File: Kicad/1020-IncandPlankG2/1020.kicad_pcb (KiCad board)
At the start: 2 copper layers, 50 x 65 mm, 33 parts, among them J1 Conn_01x22, P1 CONN_4X2, P10 CONN_2, P11 SPADE_187, P2 CONN_4X2, P3 CONN_4, P4 TST, P5 TST, P6 TST, P7 TST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

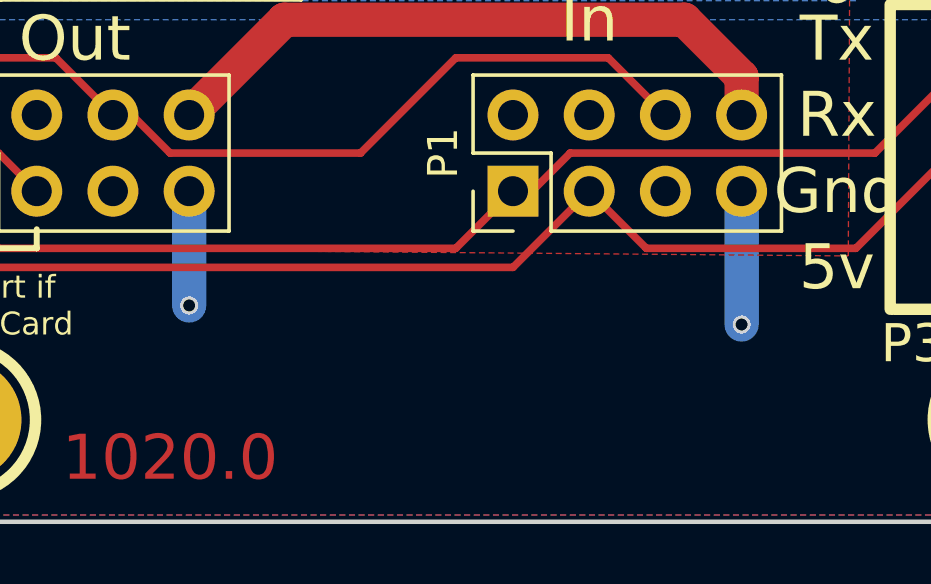
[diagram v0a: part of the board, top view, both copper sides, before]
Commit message: SolPlank:  Increase via size to meet DFM minimum.  Update build.bat to save to 1019.zip.  Add build_notes.txt to describe setting up Kicad libraries, and creating Gerbers.  Add 1019.zip for ease of ordering PCBs.
IncandPlank:  Increase via size to meet DFM minimum.  Update build.bat to save to 1020.zip.  Add build_notes.txt to describe setting up Kicad libraries, and creating Gerbers.  Add 1019.zip for ease of ordering PCBs.

VH:  Last updates grabbed from machine before sending to Joe.
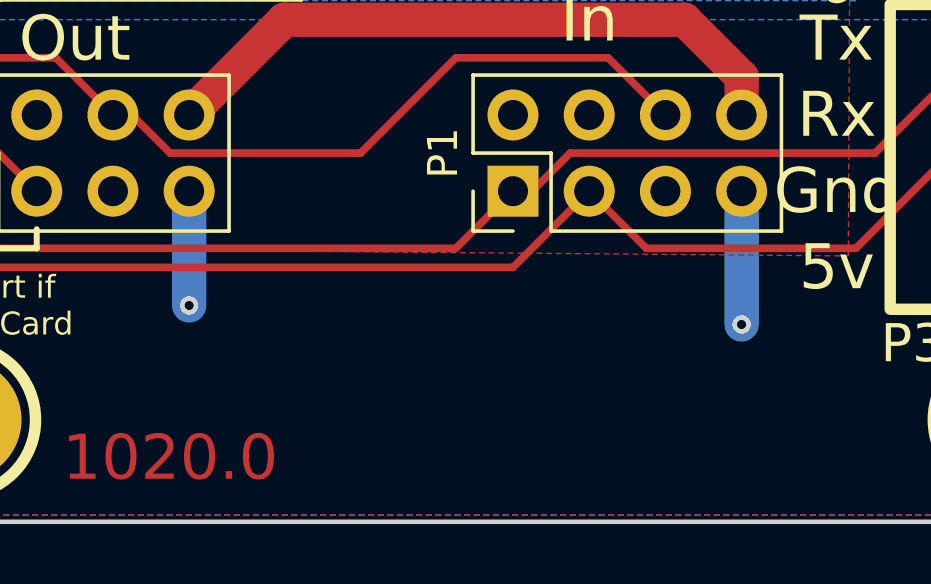
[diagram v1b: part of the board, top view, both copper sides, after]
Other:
- net class Default: via_dia 0.6 -> 0.6096; via_drill 0.4 -> 0.3048
- rule via_min_drill: 0.3 -> 0.3048
- rule via_min_size: 0.4 -> 0.6096
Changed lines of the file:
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@@
     (segment_width 0.2)
     (edge_width 0.15)
-    (via_size 0.6)
-    (via_drill 0.4)
-    (via_min_size 0.4)
-    (via_min_drill 0.3)
+    (via_size 0.6096)
+    (via_drill 0.3048)
+    (via_min_size 0.6096)
+    (via_min_drill 0.3048)
     (uvia_size 0.3)
     (uvia_drill 0.1)
@@
     (visible_elements 7FFFFFFF)
     (pcbplotparams
-      (layerselection 0x00030_80000001)
-      (usegerberextensions false)
-      (excludeedgelayer true)
+      (layerselection 0x000f0_80000001)
+      (usegerberextensions true)
+      (excludeedgelayer false)
       (linewidth 0.100000)
       (plotframeref false)
@@
       (outputformat 1)
       (mirror false)
-      (drillshape 1)
+      (drillshape 0)
       (scaleselection 1)
-      (outputdirectory ""))
+      (outputdirectory Gerber/))
   )
   (net 0 "")
@@
     (clearance 0.2)
     (trace_width 0.25)
-    (via_dia 0.6)
-    (via_drill 0.4)
+    (via_dia 0.6096)
+    (via_drill 0.3048)
     (uvia_dia 0.3)
     (uvia_drill 0.1)
@@
   (segment (start 142.24 46.99) (end 146.05 50.8) (width 0.254) (layer F.Cu) (net 21))
   (segment (start 148.59 93.98) (end 148.59 98.425) (width 1.143) (layer B.Cu) (net 23))
-  (via (at 148.59 98.425) (size 0.6) (drill 0.4) (layers F.Cu B.Cu) (net 23))
+  (via (at 148.59 98.425) (size 0.6096) (drill 0.3048) (layers F.Cu B.Cu) (net 23))
   (segment (start 130.175 93.98) (end 130.175 97.79) (width 1.143) (layer B.Cu) (net 23))
-  (via (at 130.175 97.79) (size 0.6) (drill 0.4) (layers F.Cu B.Cu) (net 23))
+  (via (at 130.175 97.79) (size 0.6096) (drill 0.3048) (layers F.Cu B.Cu) (net 23))
   (segment (start 140.97 93.98) (end 141.605 93.98) (width 0.254) (layer F.Cu) (net 24))
   (segment (start 141.605 93.98) (end 142.875 92.71) (width 0.254) (layer F.Cu) (net 24))
